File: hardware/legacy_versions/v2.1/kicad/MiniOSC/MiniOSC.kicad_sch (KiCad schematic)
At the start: 68 parts, among them J1 SYNC_IN, J10 FM_IN, J11 PWM_CV, J12 TRI_OUT, J13 SAW_OUT, J14 PULSE_OUT, J2 Conn_01x10_Pin, J9 VOCT_IN, Q1 BC549, Q2 BC559, SW1 SW_DPDT_x2, U1 40106, U2 TL074, U3 TL074

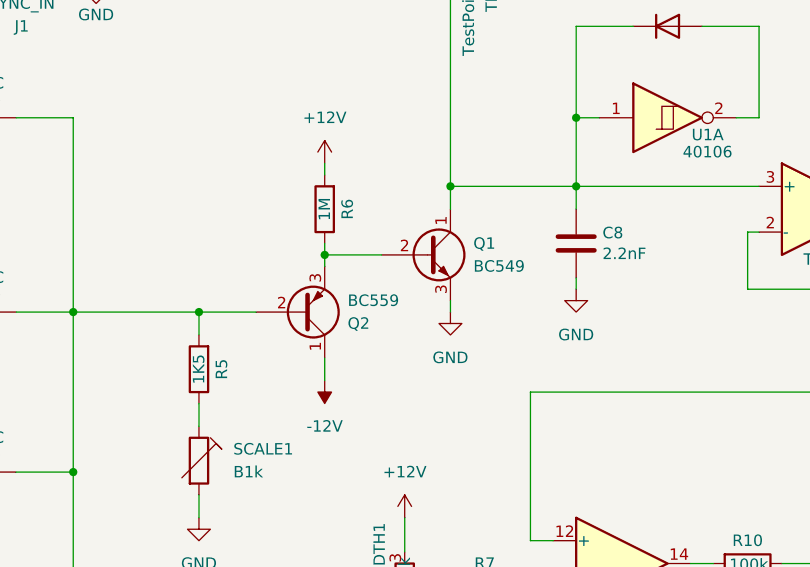
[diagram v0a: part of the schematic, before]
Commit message: Test PCB for v2.1.1 with throughole parts
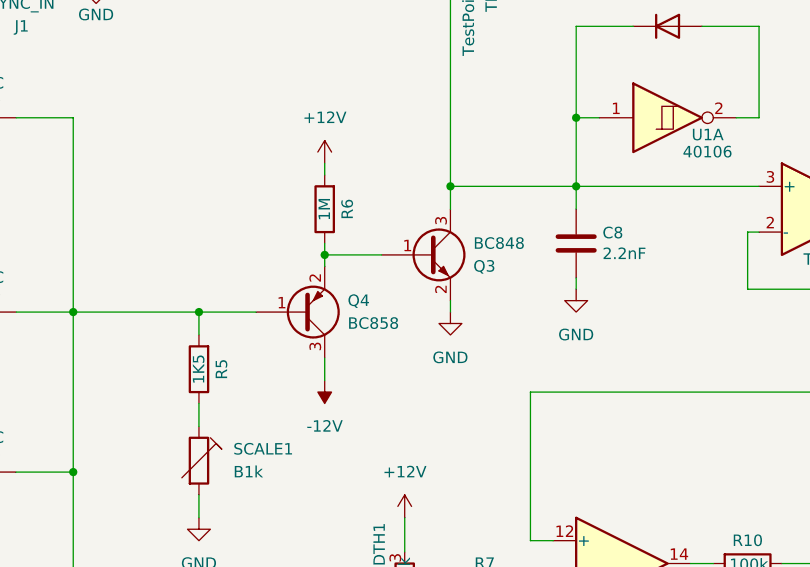
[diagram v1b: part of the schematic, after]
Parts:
- removed Q1: BC549, Package_TO_SOT_THT:TO-92_Inline_Wide, symbol Transistor_BJT:BC549
- removed Q2: BC559, Package_TO_SOT_THT:TO-92_Inline_Wide, symbol Transistor_BJT:BC559
- added Q3: BC848, Package_TO_SOT_SMD:SOT-23, symbol Transistor_BJT:BC848
- added Q4: BC858, Package_TO_SOT_SMD:SOT-23, symbol Transistor_BJT:BC858
- TH1, TH2, TH3, TH4: footprint Capacitor_THT:C_Disc_D3.8mm_W2.6mm_P2.50mm -> Resistor_SMD:R_0805_2012Metric_Pad1.20x1.40mm_HandSolder; Manufacturer (none) -> Vishay / BC Components; Part # (none) -> NTCS0603E3103JLT; URL https://mou.sr/3UrqQmM -> https://mou.sr/4el3hDO
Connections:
- net -12V: now also Q4.3 (C)
- net GND: now also Q3.2 (E)
- net at FM_AMT1.1, FM_AMT1.2, R5.2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: now also Q4.1 (B)
- net at R6.1: now also Q3.1 (B), Q4.2 (E)
- net at C8.1, D3.1 (K), SW1.3 (C)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: now also Q3.3 (C)
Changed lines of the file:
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@@
 	(title_block
 		(title "MiniOSC")
-		(rev "2.1.1")
+		(rev "2.1")
 		(company "benjiaomodular")
 	)
@@
 			)
 		)
-		(property "Footprint" "Capacitor_THT:C_Disc_D3.8mm_W2.6mm_P2.50mm"
+		(property "Footprint" "Resistor_SMD:R_0805_2012Metric_Pad1.20x1.40mm_HandSolder"
 			(at 44.45 104.14 0)
 			(effects
@@
 			)
 		)
-		(property "URL" "https://mou.sr/3UrqQmM"
+		(property "URL" "https://mou.sr/4el3hDO"
 			(at 44.45 104.14 0)
 			(effects
@@
 			)
 		)
-		(property "Manufacturer" ""
+		(property "Manufacturer" "Vishay / BC Components"
 			(at 44.45 104.14 0)
 			(effects
@@
 			)
 		)
-		(property "Part #" ""
+		(property "Part #" "NTCS0603E3103JLT"
 			(at 44.45 104.14 0)
 			(effects
@@
 			)
 		)
-		(property "Footprint" "Capacitor_THT:C_Disc_D3.8mm_W2.6mm_P2.50mm"
+		(property "Footprint" "Resistor_SMD:R_0805_2012Metric_Pad1.20x1.40mm_HandSolder"
 			(at 52.07 83.82 0)
 			(effects
@@
 			)
 		)
-		(property "URL" "https://mou.sr/3UrqQmM"
+		(property "URL" "https://mou.sr/4el3hDO"
 			(at 52.07 83.82 0)
 			(effects
@@
 			)
 		)
-		(property "Manufacturer" ""
+		(property "Manufacturer" "Vishay / BC Components"
 			(at 52.07 83.82 0)
 			(effects
@@
 			)
 		)
-		(property "Part #" ""
+		(property "Part #" "NTCS0603E3103JLT"
 			(at 52.07 83.82 0)
 			(effects
@@
 			)
 		)
-		(property "Footprint" "Capacitor_THT:C_Disc_D3.8mm_W2.6mm_P2.50mm"
+		(property "Footprint" "Resistor_SMD:R_0805_2012Metric_Pad1.20x1.40mm_HandSolder"
 			(at 52.07 66.04 0)
 			(effects
@@
 			)
 		)
-		(property "URL" "https://mou.sr/3UrqQmM"
+		(property "URL" "https://mou.sr/4el3hDO"
 			(at 52.07 66.04 0)
 			(effects
@@
 			)
 		)
-		(property "Manufacturer" ""
+		(property "Manufacturer" "Vishay / BC Components"
 			(at 52.07 66.04 0)
 			(effects
@@
 			)
 		)
-		(property "Part #" ""
+		(property "Part #" "NTCS0603E3103JLT"
 			(at 52.07 66.04 0)
 			(effects
@@
 			)
 		)
-		(property "Footprint" "Capacitor_THT:C_Disc_D3.8mm_W2.6mm_P2.50mm"
+		(property "Footprint" "Resistor_SMD:R_0805_2012Metric_Pad1.20x1.40mm_HandSolder"
 			(at 52.07 44.45 0)
 			(effects
@@
 			)
 		)
-		(property "URL" "https://mou.sr/3UrqQmM"
+		(property "URL" "https://mou.sr/4el3hDO"
 			(at 52.07 44.45 0)
 			(effects
@@
 			)
 		)
-		(property "Manufacturer" ""
+		(property "Manufacturer" "Vishay / BC Components"
 			(at 52.07 44.45 0)
 			(effects
@@
 			)
 		)
-		(property "Part #" ""
+		(property "Part #" "NTCS0603E3103JLT"
 			(at 52.07 44.45 0)
 			(effects
@@
 	)
 	(symbol
-		(lib_id "Transistor_BJT:BC559")
-		(at 88.9 66.04 0)
-		(mirror x)
-		(unit 1)
-		(exclude_from_sim no)
-		(in_bom yes)
-		(on_board yes)
-		(dnp no)
-		(property "Reference" "Q2"
-			(at 93.98 67.3101 0)
-			(effects
-				(font
-					(size 1.27 1.27)
-				)
-				(justify left)
-			)
-		)
-		(property "Value" "BC559"
-			(at 93.98 64.7701 0)
-			(effects
-				(font
-					(size 1.27 1.27)
-				)
-				(justify left)
-			)
-		)
-		(property "Footprint" "Package_TO_SOT_THT:TO-92_Inline_Wide"
-			(at 93.98 64.135 0)
-			(effects
-				(font
-					(size 1.27 1.27)
-					(italic yes)
-				)
-				(justify left)
-				(hide yes)
-			)
-		)
-		(property "Datasheet" "https://www.onsemi.com/pub/Collateral/BC556BTA-D.pdf"
-			(at 88.9 66.04 0)
-			(effects
-				(font
-					(size 1.27 1.27)
-				)
-				(justify left)
-				(hide yes)
-			)
-		)
-		(property "Description" "0.1A Ic, 30V Vce, PNP Small Signal Transistor, TO-92"
-			(at 88.9 66.04 0)
-			(effects
-				(font
-					(size 1.27 1.27)
-				)
-				(hide yes)
-			)
-		)
-		(pin "2"
-		)
-		(pin "3"
-		)
-		(pin "1"
-		)
-		(instances
-			(project ""
-				(path "/995d0ac4-fdc3-404c-a472-c60e34c20729"
-					(reference "Q2")
-					(unit 1)
-				)
-			)
-		)
-	)
-	(symbol
 		(lib_id "Device:R")
 		(at 81.28 25.4 270)
@@
 	)
 	(symbol
+		(lib_id "Transistor_BJT:BC848")
+		(at 102.87 59.69 0)
+		(unit 1)
+		(exclude_from_sim no)
+		(in_bom yes)
+		(on_board yes)
+		(dnp no)
+		(property "Reference" "Q3"
+			(at 107.95 60.9601 0)
+			(effects
+				(font
+					(size 1.27 1.27)
+				)
+				(justify left)
+			)
+		)
+		(property "Value" "BC848"
+			(at 107.95 58.4201 0)
+			(effects
+				(font
+					(size 1.27 1.27)
+				)
+				(justify left)
+			)
+		)
+		(property "Footprint" "Package_TO_SOT_SMD:SOT-23"
+			(at 107.95 61.595 0)
+			(effects
+				(font
+					(size 1.27 1.27)
+					(italic yes)
+				)
+				(justify left)
+				(hide yes)
+			)
+		)
+		(property "Datasheet" "http://www.infineon.com/dgdl/Infineon-BC847SERIES_BC848SERIES_BC849SERIES_BC850SERIES-DS-v01_01-en.pdf?fileId=db3a304314dca389011541d4630a1657"
+			(at 102.87 59.69 0)
+			(effects
+				(font
+					(size 1.27 1.27)
+				)
+				(justify left)
+				(hide yes)
+			)
+		)
+		(property "Description" "0.1A Ic, 30V Vce, NPN Transistor, SOT-23"
+			(at 102.87 59.69 0)
+			(effects
+				(font
+					(size 1.27 1.27)
+				)
+				(hide yes)
+			)
+		)
+		(property "URL" "https://mou.sr/3B2EAO3"
+			(at 102.87 59.69 0)
+			(effects
+				(font
+					(size 1.27 1.27)
+				)
+				(hide yes)
+			)
+		)
+		(property "Manufacturer" "onsemi"
+			(at 102.87 59.69 0)
+			(effects
+				(font
+					(size 1.27 1.27)
+				)
+				(hide yes)
+			)
+		)
+		(property "Part #" "BC848ALT1G"
+			(at 102.87 59.69 0)
+			(effects
+				(font
+					(size 1.27 1.27)
+				)
+				(hide yes)
+			)
+		)
+		(pin "1"
+		)
+		(pin "2"
+		)
+		(pin "3"
+		)
+		(instances
+			(project ""
+				(path "/995d0ac4-fdc3-404c-a472-c60e34c20729"
+					(reference "Q3")
+					(unit 1)
+				)
+			)
+		)
+	)
+	(symbol
 		(lib_id "power:GND")
 		(at 237.49 154.94 0)
@@
 	)
 	(symbol
-		(lib_id "Transistor_BJT:BC549")
-		(at 102.87 59.69 0)
-		(unit 1)
-		(exclude_from_sim no)
-		(in_bom yes)
-		(on_board yes)
-		(dnp no)
-		(fields_autoplaced yes)
-		(property "Reference" "Q1"
-			(at 107.95 58.4199 0)
-			(effects
-				(font
-					(size 1.27 1.27)
-				)
-				(justify left)
-			)
-		)
-		(property "Value" "BC549"
-			(at 107.95 60.9599 0)
-			(effects
-				(font
-					(size 1.27 1.27)
-				)
-				(justify left)
-			)
-		)
-		(property "Footprint" "Package_TO_SOT_THT:TO-92_Inline_Wide"
-			(at 107.95 61.595 0)
-			(effects
-				(font
-					(size 1.27 1.27)
-					(italic yes)
-				)
-				(justify left)
-				(hide yes)
-			)
-		)
-		(property "Datasheet" "https://www.onsemi.com/pub/Collateral/BC550-D.pdf"
-			(at 102.87 59.69 0)
-			(effects
-				(font
-					(size 1.27 1.27)
-				)
-				(justify left)
-				(hide yes)
-			)
-		)
-		(property "Description" "0.1A Ic, 30V Vce, Small Signal NPN Transistor, TO-92"
-			(at 102.87 59.69 0)
-			(effects
-				(font
-					(size 1.27 1.27)
-				)
-				(hide yes)
-			)
-		)
-		(pin "1"
-		)
-		(pin "2"
-		)
-		(pin "3"
-		)
-		(instances
-			(project ""
-				(path "/995d0ac4-fdc3-404c-a472-c60e34c20729"
-					(reference "Q1")
-					(unit 1)
-				)
-			)
-		)
-	)
-	(symbol
 		(lib_id "Device:R")
 		(at 109.22 96.52 270)
@@
 					(unit 1)
 				)
+			)
+		)
+	)
+	(symbol
+		(lib_id "Transistor_BJT:BC858")
+		(at 88.9 66.04 0)
+		(mirror x)
+		(unit 1)
+		(exclude_from_sim no)
+		(in_bom yes)
+		(on_board yes)
+		(dnp no)
+		(fields_autoplaced yes)
+		(property "Reference" "Q4"
+			(at 93.98 64.7699 0)
+			(effects
+				(font
+					(size 1.27 1.27)
+				)
+				(justify left)
+			)
+		)
+		(property "Value" "BC858"
+			(at 93.98 67.3099 0)
+			(effects
+				(font
+					(size 1.27 1.27)
+				)
+				(justify left)
+			)
+		)
+		(property "Footprint" "Package_TO_SOT_SMD:SOT-23"
+			(at 93.98 64.135 0)
+			(effects
+				(font
+					(size 1.27 1.27)
+					(italic yes)
+				)
+				(justify left)
+				(hide yes)
+			)
+		)
+		(property "Datasheet" "https://www.onsemi.com/pub/Collateral/BC860-D.pdf"
+			(at 88.9 66.04 0)
+			(effects
+				(font
+					(size 1.27 1.27)
+				)
+				(justify left)
+				(hide yes)
+			)
+		)
+		(property "Description" "0.1A Ic, 30V Vce, PNP Transistor, SOT-23"
+			(at 88.9 66.04 0)
+			(effects
+				(font
+					(size 1.27 1.27)
+				)
+				(hide yes)
+			)
+		)
+		(property "URL" "https://mou.sr/3ZkYkq0"
+			(at 88.9 66.04 0)
+			(effects
+				(font
+					(size 1.27 1.27)
+				)
+				(hide yes)
+			)
+		)
+		(property "Manufacturer" "onsemi"
+			(at 88.9 66.04 0)
+			(effects
+				(font
+					(size 1.27 1.27)
+				)
+				(hide yes)
+			)
+		)
+		(property "Part #" "BC858CLT3G"
+			(at 88.9 66.04 0)
+			(effects
+				(font
+					(size 1.27 1.27)
+				)
+				(hide yes)
+			)
+		)
+		(pin "1"
+		)
+		(pin "3"
+		)
+		(pin "2"
+		)
+		(instances
+			(project ""
+				(path "/995d0ac4-fdc3-404c-a472-c60e34c20729"
+					(reference "Q4")
+					(unit 1)
+				)
